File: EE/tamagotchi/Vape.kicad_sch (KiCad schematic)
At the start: 1 part, among them J1 Conn_01x02_Pin

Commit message: Generic Continutation Checkin
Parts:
- added SW2: SW_SPST, symbol Switch:SW_SPST
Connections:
- new net GND: SW2.1 (A)
- new net VAPE_SW: SW2.2 (B)
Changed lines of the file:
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@@
 	(generator_version "9.0")
 	(paper "A4")
+	(label "VAPE_EN"
+		(at 22.86 16.51 0)
+		(effects
+			(font
+				(size 1.27 1.27)
+			)
+			(justify left bottom)
+		)
+	)
+	(label "VAPE_SW"
+		(at 173.99 139.7 180)
+		(effects
+			(font
+				(size 1.27 1.27)
+			)
+			(justify right bottom)
+		)
+	)
+	(label "VAPE_SW"
+		(at 274.32 15.24 180)
+		(effects
+			(font
+				(size 1.27 1.27)
+			)
+			(justify right bottom)
+		)
+	)
 	(label "UT_OUT-"
 		(at 265.43 99.06 270)
@@
 		)
 	)
+	(hierarchical_label "VAPE_SW"
+		(shape input)
+		(at 274.32 15.24 0)
+		(effects
+			(font
+				(size 1.27 1.27)
+			)
+			(justify left)
+		)
+	)
+	(hierarchical_label "VAPE_EN"
+		(shape input)
+		(at 22.86 16.51 180)
+		(effects
+			(font
+				(size 1.27 1.27)
+			)
+			(justify right)
+		)
+	)
+	(symbol
+		(lib_id "Switch:SW_SPST")
+		(at 173.99 144.78 90)
+		(unit 1)
+		(exclude_from_sim no)
+		(in_bom yes)
+		(on_board yes)
+		(dnp no)
+		(fields_autoplaced yes)
+		(property "Reference" "SW2"
+			(at 175.26 143.5099 90)
+			(effects
+				(font
+					(size 1.27 1.27)
+				)
+				(justify right)
+			)
+		)
+		(property "Value" "SW_SPST"
+			(at 175.26 146.0499 90)
+			(effects
+				(font
+					(size 1.27 1.27)
+				)
+				(justify right)
+			)
+		)
+		(property "Footprint" ""
+			(at 173.99 144.78 0)
+			(effects
+				(font
+					(size 1.27 1.27)
+				)
+				(hide yes)
+			)
+		)
+		(property "Datasheet" "~"
+			(at 173.99 144.78 0)
+			(effects
+				(font
+					(size 1.27 1.27)
+				)
+				(hide yes)
+			)
+		)
+		(property "Description" "Single Pole Single Throw (SPST) switch"
+			(at 173.99 144.78 0)
+			(effects
+				(font
+					(size 1.27 1.27)
+				)
+				(hide yes)
+			)
+		)
+		(pin "1"
+		)
+		(pin "2"
+		)
+		(instances
+			(project ""
+				(path "/47ffaef6-4682-4a87-a393-bad1a10963be/c5f463fe-c05b-4af3-8646-c22a17ba3c4f"
+					(reference "SW2")
+					(unit 1)
+				)
+			)
+		)
+	)
+	(symbol
+		(lib_id "power:GND")
+		(at 173.99 149.86 0)
+		(unit 1)
+		(exclude_from_sim no)
+		(in_bom yes)
+		(on_board yes)
+		(dnp no)
+		(fields_autoplaced yes)
+		(property "Reference" "#PWR021"
+			(at 173.99 156.21 0)
+			(effects
+				(font
+					(size 1.27 1.27)
+				)
+				(hide yes)
+			)
+		)
+		(property "Value" "GND"
+			(at 173.99 154.94 0)
+			(effects
+				(font
+					(size 1.27 1.27)
+				)
+			)
+		)
+		(property "Footprint" ""
+			(at 173.99 149.86 0)
+			(effects
+				(font
+					(size 1.27 1.27)
+				)
+				(hide yes)
+			)
+		)
+		(property "Datasheet" ""
+			(at 173.99 149.86 0)
+			(effects
+				(font
+					(size 1.27 1.27)
+				)
+				(hide yes)
+			)
+		)
+		(property "Description" "Power symbol creates a global label with name \"GND\" , ground"
+			(at 173.99 149.86 0)
+			(effects
+				(font
+					(size 1.27 1.27)
+				)
+				(hide yes)
+			)
+		)
+		(pin "1"
+		)
+		(instances
+			(project ""
+				(path "/47ffaef6-4682-4a87-a393-bad1a10963be/c5f463fe-c05b-4af3-8646-c22a17ba3c4f"
+					(reference "#PWR021")
+					(unit 1)
+				)
+			)
+		)
+	)

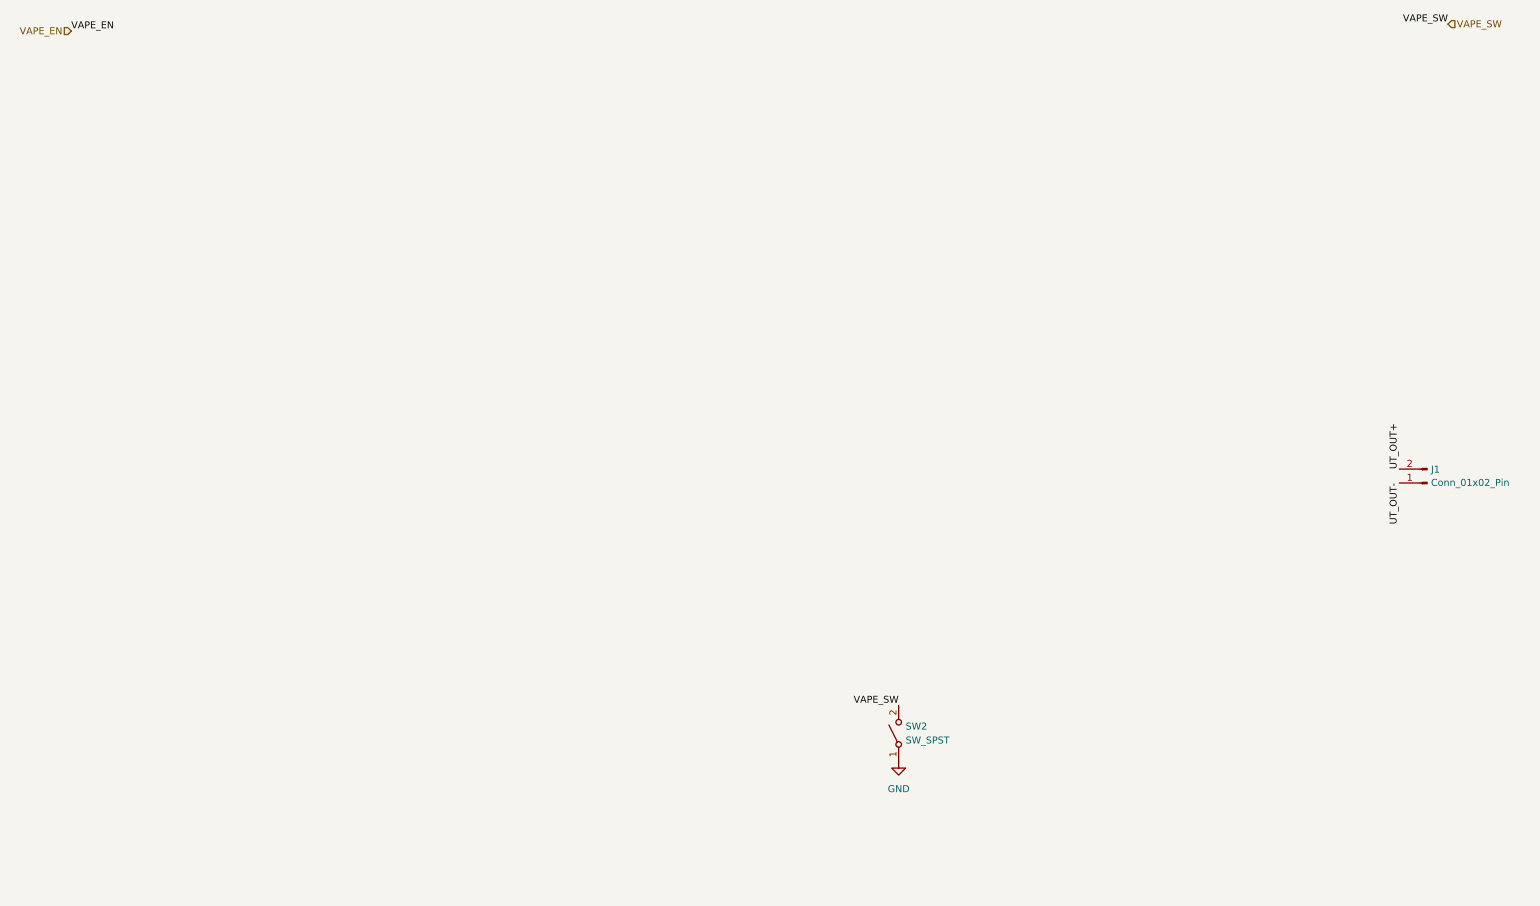
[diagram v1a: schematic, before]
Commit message: WIP - added 3D / footprints for devices. RGY LEDs aren't right
Need to do more outling / ect. super rough placement for everything.
LED footprint for RGY appears just wrong
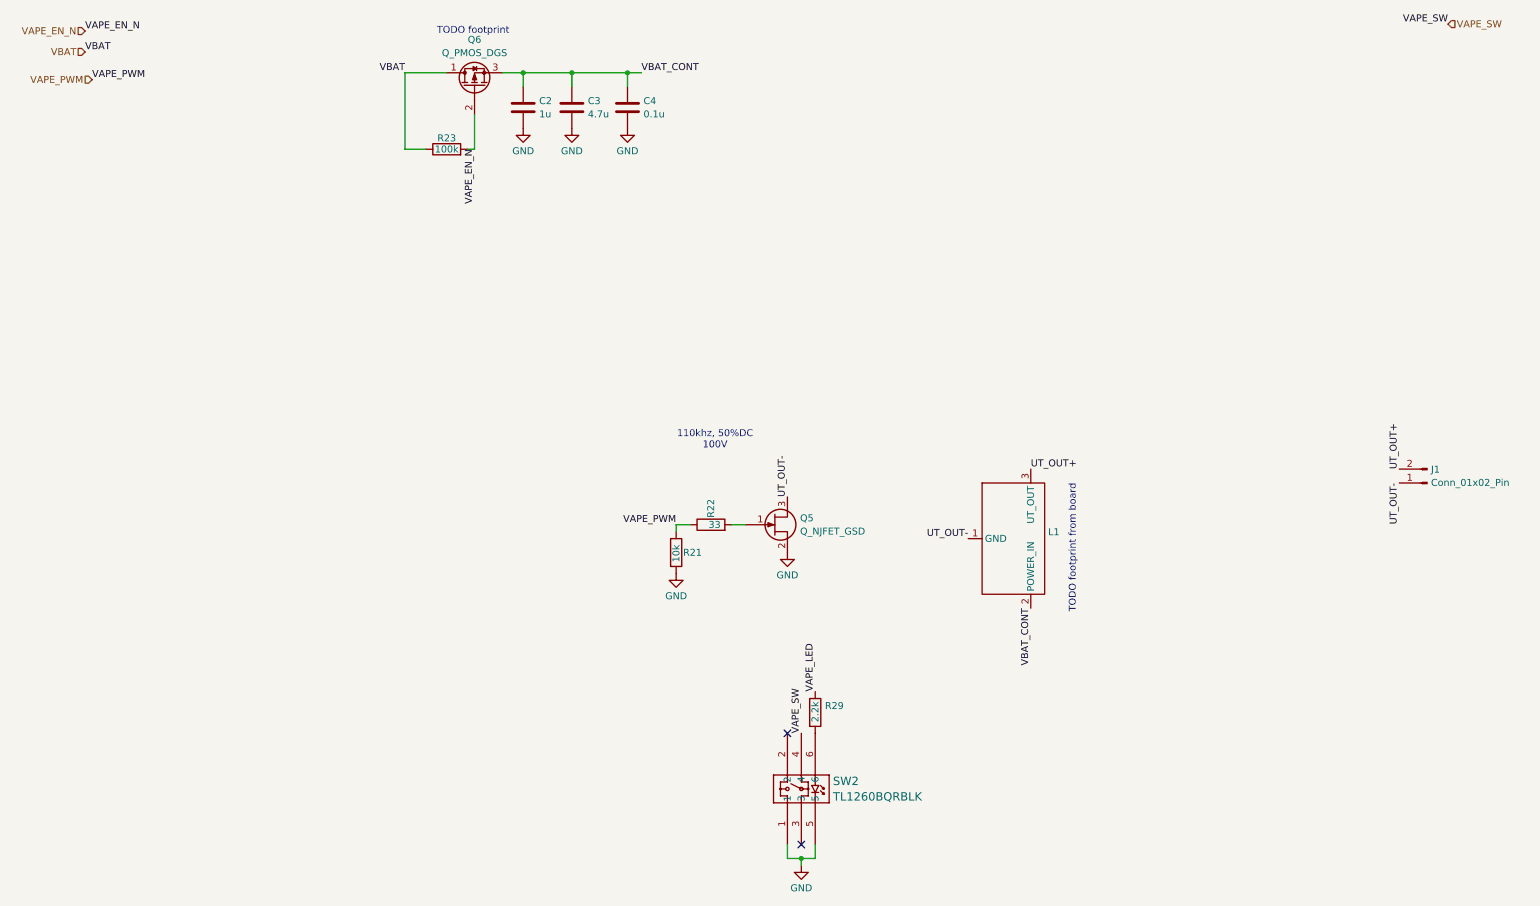
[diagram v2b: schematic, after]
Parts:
- removed SW2: SW_SPST, symbol Switch:SW_SPST
- added C2: 1u, Capacitor_SMD:C_0402_1005Metric_Pad0.74x0.62mm_HandSolder, symbol Device:C
- added C3: 4.7u, Capacitor_SMD:C_0402_1005Metric_Pad0.74x0.62mm_HandSolder, symbol Device:C
- added C4: 0.1u, Capacitor_SMD:C_0402_1005Metric_Pad0.74x0.62mm_HandSolder, symbol Device:C
- added L1: ~, symbol New_Library:Txformer
- added Q5: Q_NJFET_GSD, symbol Device:Q_NJFET_GSD
- added Q6: Q_PMOS_DGS, symbol Transistor_FET:Q_PMOS_DGS
- added R21: 10k, Resistor_SMD:R_0402_1005Metric_Pad0.72x0.64mm_HandSolder, symbol Device:R
- added R22: 33, Resistor_SMD:R_0402_1005Metric_Pad0.72x0.64mm_HandSolder, symbol Device:R
- added R23: 100k, Resistor_SMD:R_0402_1005Metric_Pad0.72x0.64mm_HandSolder, symbol Device:R
- added R29: 2.2k, Resistor_SMD:R_0402_1005Metric_Pad0.72x0.64mm_HandSolder, symbol Device:R
- added SW2: TL1260BQRBLK, Library:TL1260_EWI, symbol New_Library:TL1260BQRBLK
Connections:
- net GND: now also C2.2, C3.2, C4.2, Q5.2 (S), R21.2, SW2.1, SW2.5
- net UT_OUT+: now also L1.3 (UT_OUT)
- net UT_OUT-: now also L1.1 (GND), Q5.3 (D)
- net VAPE_SW: now also SW2.4
- new net: Q5.1 (G), R22.2
- new net: R29.2, SW2.6
- new net VAPE_EN_N: Q6.2 (G), R23.2
- new net VAPE_LED: R29.1
- new net VAPE_PWM: R21.1, R22.1
- new net VBAT: Q6.1 (D), R23.1
- new net VBAT_CONT: C2.1, C3.1, C4.1, L1.2 (POWER_IN), Q6.3 (S)
- no-connect marks 0 -> 2
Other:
- note added: "110khz, 50%DC 100V"
- note added: "TODO footprint"
- note added: "TODO footprint from board"

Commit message: Footprints and mechanical parts assigned
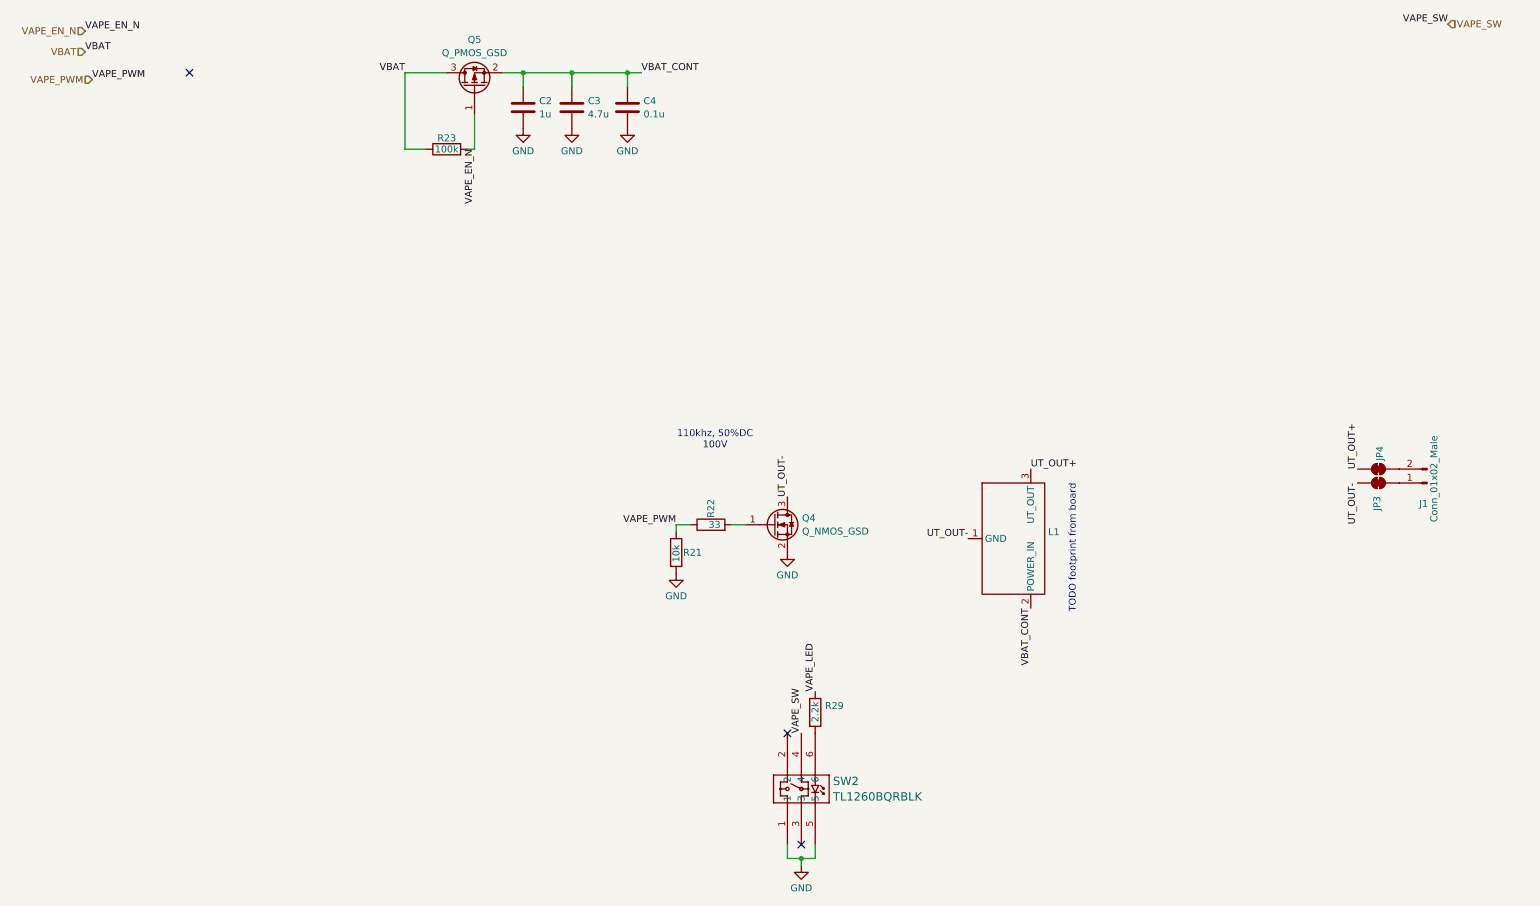
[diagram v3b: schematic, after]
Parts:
- removed J1: Conn_01x02_Pin, symbol Connector:Conn_01x02_Pin
- removed Q5: Q_NJFET_GSD, symbol Device:Q_NJFET_GSD
- removed Q6: Q_PMOS_DGS, symbol Transistor_FET:Q_PMOS_DGS
- added J1: Conn_01x02_Male, Connector_JST:JST_PH_B2B-PH-K_1x02_P2.00mm_Vertical, symbol Connector:Conn_01x02_Male
- added JP3, JP4: SolderJumper_2_Bridged, Jumper:SolderJumper-2_P1.3mm_Bridged2Bar_RoundedPad1.0x1.5mm, symbol Jumper:SolderJumper_2_Bridged
- added Q4: Q_NMOS_GSD, Package_TO_SOT_SMD:SOT-23, symbol Transistor_FET:Q_NMOS_GSD
- added Q5: Q_PMOS_GSD, Package_TO_SOT_SMD:SOT-23, symbol Transistor_FET:Q_PMOS_GSD
- L1: footprint (none) -> Library:UT Transformer
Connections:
- net GND: now also Q4.2 (S)
- net UT_OUT+: now also JP4.1 (A)
- net UT_OUT-: now also JP3.2 (B), Q4.3 (D)
- net VAPE_EN_N: now also Q5.1 (G)
- net VBAT: now also Q5.3 (D)
- net VBAT_CONT: now also Q5.2 (S)
- net at R22.2: now also Q4.1 (G)
- new net: J1.1 (Pin_1), JP3.1 (A)
- new net: J1.2 (Pin_2), JP4.2 (B)
- no-connect marks 2 -> 3
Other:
- note removed: "TODO footprint"

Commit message: Minor Placement update
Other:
- note added: "110khz, 50%DC 100V Consumes ~200mA @ 5V"
- note removed: "110khz, 50%DC 100V"
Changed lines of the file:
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@@
 	(generator_version "9.0")
 	(paper "A4")
-	(text "110khz, 50%DC\n100V"
+	(text "110khz, 50%DC\n100V\n\nConsumes ~200mA @ 5V"
 		(exclude_from_sim no)
-		(at 140.462 91.186 0)
+		(at 126.746 87.122 0)
 		(effects
 			(font

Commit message: Removed LEDs
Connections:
- no-connect marks 3 -> 2
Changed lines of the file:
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@@
-	)
-	(no_connect
-		(at 44.45 24.13)
 	)
 	(no_connect
@@
 	(label "UT_OUT+"
 		(at 198.12 96.52 0)
+		(effects
+			(font
+				(size 1.27 1.27)
+			)
+			(justify left bottom)
+		)
+	)
+	(label "VAPE_LED"
+		(at 26.67 30.48 0)
 		(effects
 			(font
@@
 		)
 	)
+	(hierarchical_label "VAPE_LED"
+		(shape input)
+		(at 26.67 30.48 180)
+		(effects
+			(font
+				(size 1.27 1.27)
+			)
+			(justify right)
+		)
+	)

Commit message: Silkscreen Fix
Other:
- note removed: "TODO footprint from board"
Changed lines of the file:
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@@
-		)
-	)
-	(text "TODO footprint from board"
-		(exclude_from_sim no)
-		(at 205.74 110.998 90)
-		(effects
-			(font
-				(size 1.27 1.27)
-			)
 		)
 	)

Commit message: Adding some new requirements for pressure / air flow
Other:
- note added: "TODO pressure sensor?"
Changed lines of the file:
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@@
 	(generator_version "9.0")
 	(paper "A4")
+	(text "TODO pressure sensor?"
+		(exclude_from_sim no)
+		(at 69.596 92.71 0)
+		(effects
+			(font
+				(size 1.27 1.27)
+			)
+		)
+	)
 	(text "110khz, 50%DC\n100V\n\nConsumes ~200mA @ 5V"
 		(exclude_from_sim no)
-		(at 126.746 87.122 0)
+		(at 264.668 78.74 0)
 		(effects
 			(font

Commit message: Added pressure sensor. Re laid out board
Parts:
- removed JP3, JP4: SolderJumper_2_Bridged, Jumper:SolderJumper-2_P1.3mm_Bridged2Bar_RoundedPad1.0x1.5mm, symbol Jumper:SolderJumper_2_Bridged
- J1: footprint Connector_JST:JST_PH_B2B-PH-K_1x02_P2.00mm_Vertical -> Connector_JST:JST_PH_S2B-PH-SM4-TB_1x02-1MP_P2.00mm_Horizontal
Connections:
- net UT_OUT+: now also J1.2 (Pin_2)
- net UT_OUT-: now also J1.1 (Pin_1)
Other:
- note removed: "TODO pressure sensor?"
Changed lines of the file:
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@@
 	(generator_version "9.0")
 	(paper "A4")
-	(text "TODO pressure sensor?"
-		(exclude_from_sim no)
-		(at 69.596 92.71 0)
-		(effects
-			(font
-				(size 1.27 1.27)
-			)
-		)
-	)
 	(text "110khz, 50%DC\n100V\n\nConsumes ~200mA @ 5V"
 		(exclude_from_sim no)
@@
 	)
 	(label "UT_OUT-"
-		(at 257.81 99.06 270)
+		(at 265.43 99.06 270)
 		(effects
 			(font
@@
 	)
 	(label "UT_OUT+"
-		(at 257.81 96.52 90)
+		(at 265.43 96.52 90)
 		(effects
 			(font
@@
 			)
 		)
-		(property "Footprint" "Connector_JST:JST_PH_B2B-PH-K_1x02_P2.00mm_Vertical"
+		(property "Footprint" "Connector_JST:JST_PH_S2B-PH-SM4-TB_1x02-1MP_P2.00mm_Horizontal"
 			(at 270.51 99.06 0)
 			(effects
@@
 	)
 	(symbol
-		(lib_id "Jumper:SolderJumper_2_Bridged")
-		(at 261.62 96.52 0)
-		(unit 1)
-		(exclude_from_sim no)
-		(in_bom no)
-		(on_board yes)
-		(dnp no)
-		(property "Reference" "JP4"
-			(at 261.874 94.996 90)
-			(effects
-				(font
-					(size 1.27 1.27)
-				)
-				(justify left)
-			)
-		)
-		(property "Value" "SolderJumper_2_Bridged"
-			(at 262.8321 94.869 90)
-			(effects
-				(font
-					(size 1.27 1.27)
-				)
-				(justify left)
-				(hide yes)
-			)
-		)
-		(property "Footprint" "Jumper:SolderJumper-2_P1.3mm_Bridged2Bar_RoundedPad1.0x1.5mm"
-			(at 261.62 96.52 0)
-			(effects
-				(font
-					(size 1.27 1.27)
-				)
-				(hide yes)
-			)
-		)
-		(property "Datasheet" "~"
-			(at 261.62 96.52 0)
-			(effects
-				(font
-					(size 1.27 1.27)
-				)
-				(hide yes)
-			)
-		)
-		(property "Description" "Solder Jumper, 2-pole, closed/bridged"
-			(at 261.62 96.52 0)
-			(effects
-				(font
-					(size 1.27 1.27)
-				)
-				(hide yes)
-			)
-		)
-		(property "DigikeyLink" ""
-			(at 261.62 96.52 0)
-			(effects
-				(font
-					(size 1.27 1.27)
-				)
-				(hide yes)
-			)
-		)
-		(property "MPN" ""
-			(at 261.62 96.52 0)
-			(effects
-				(font
-					(size 1.27 1.27)
-				)
-				(hide yes)
-			)
-		)
-		(pin "1"
-		)
-		(pin "2"
-		)
-		(instances
-			(project "tamagotchi"
-				(path "/47ffaef6-4682-4a87-a393-bad1a10963be/c5f463fe-c05b-4af3-8646-c22a17ba3c4f"
-					(reference "JP4")
-					(unit 1)
-				)
-			)
-		)
-	)
-	(symbol
 		(lib_id "Transistor_FET:Q_PMOS_GSD")
 		(at 96.52 26.67 90)
@@
 					(unit 1)
 				)
-			)
-		)
-	)
-	(symbol
-		(lib_id "Jumper:SolderJumper_2_Bridged")
-		(at 261.62 99.06 180)
-		(unit 1)
-		(exclude_from_sim no)
-		(in_bom no)
-		(on_board yes)
-		(dnp no)
-		(property "Reference" "JP3"
-			(at 261.366 104.14 90)
-			(effects
-				(font
-					(size 1.27 1.27)
-				)
-				(justify right)
-			)
-		)
-		(property "Value" "SolderJumper_2_Bridged"
-			(at 262.8321 97.409 90)
-			(effects
-				(font
-					(size 1.27 1.27)
-				)
-				(justify right)
-				(hide yes)
-			)
-		)
-		(property "Footprint" "Jumper:SolderJumper-2_P1.3mm_Bridged2Bar_RoundedPad1.0x1.5mm"
-			(at 261.62 99.06 0)
-			(effects
-				(font
-					(size 1.27 1.27)
-				)
-				(hide yes)
-			)
-		)
-		(property "Datasheet" "~"
-			(at 261.62 99.06 0)
-			(effects
-				(font
-					(size 1.27 1.27)
-				)
-				(hide yes)
-			)
-		)
-		(property "Description" "Solder Jumper, 2-pole, closed/bridged"
-			(at 261.62 99.06 0)
-			(effects
-				(font
-					(size 1.27 1.27)
-				)
-				(hide yes)
-			)
-		)
-		(property "DigikeyLink" ""
-			(at 261.62 99.06 0)
-			(effects
-				(font
-					(size 1.27 1.27)
-				)
-				(hide yes)
-			)
-		)
-		(property "MPN" ""
-			(at 261.62 99.06 0)
-			(effects
-				(font
-					(size 1.27 1.27)
-				)
-				(hide yes)
-			)
-		)
-		(pin "1"
-		)
-		(pin "2"
-		)
-		(instances
-			(project "tamagotchi"
-				(path "/47ffaef6-4682-4a87-a393-bad1a10963be/c5f463fe-c05b-4af3-8646-c22a17ba3c4f"
-					(reference "JP3")
-					(unit 1)
-				)
